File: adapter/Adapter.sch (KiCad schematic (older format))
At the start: 58 parts, among them J1 USB_B_Micro, J2 2040210-1, J3 USB_C_Receptacle, J4 Conn_01x05_Male, J5 Conn_01x03_Male, Q1 IRLML2244TRPBF, SW1 RESET, SW2 BOOT, U1 SN75DP119RGYT, U2 LD1117S33TR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

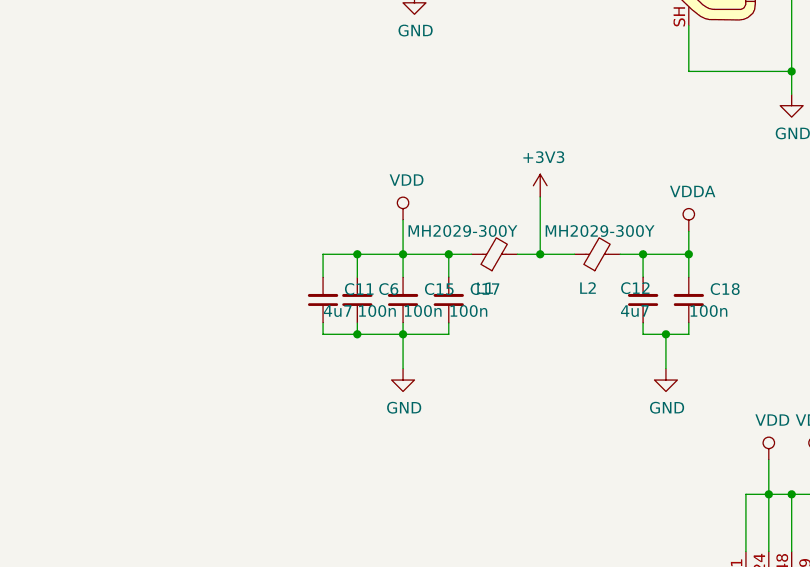
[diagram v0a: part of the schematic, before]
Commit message: shifting back some components from the USB-C jack
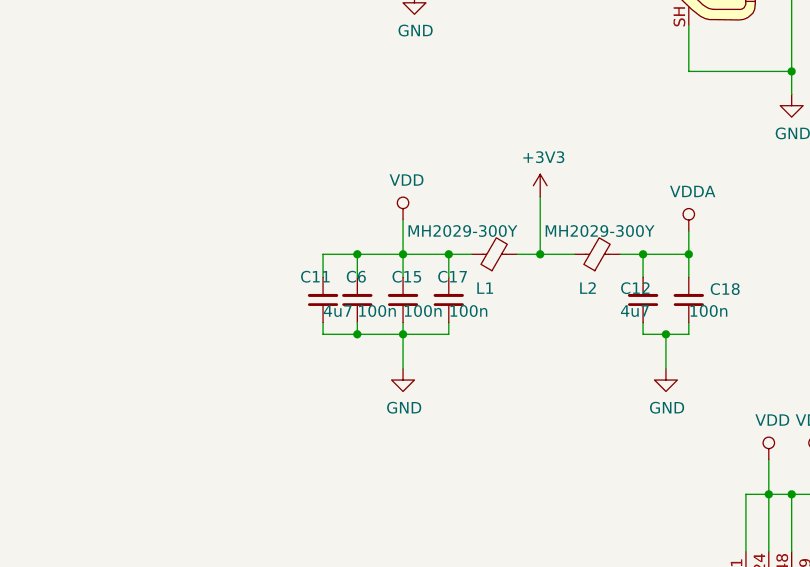
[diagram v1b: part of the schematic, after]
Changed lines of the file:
@@
 U 1 1 5C5D2103
 P 950 3150
-F 0 "C11" H 858 3104 50  0000 R CNN
+F 0 "C11" H 1050 3050 50  0000 R CNN
 F 1 "4u7" H 950 3200 50  0000 R CNN
 F 2 "Capacitor_SMD:C_0603_1608Metric_Pad1.05x0.95mm_HandSolder" H 950 3150 50  0001 C CNN
@@
 U 1 1 5C56A473
 P 1100 3150
-F 0 "C6" H 1008 3104 50  0000 R CNN
+F 0 "C6" H 1150 3050 50  0000 R CNN
 F 1 "100n" H 1100 3200 50  0000 R CNN
 F 2 "Capacitor_SMD:C_0603_1608Metric_Pad1.05x0.95mm_HandSolder" H 1100 3150 50  0001 C CNN
@@
 U 1 1 5C5EEE53
 P 1300 3150
-F 0 "C15" H 1208 3104 50  0000 R CNN
+F 0 "C15" H 1350 3050 50  0000 R CNN
 F 1 "100n" H 1300 3200 50  0000 R CNN
 F 2 "Capacitor_SMD:C_0603_1608Metric_Pad1.05x0.95mm_HandSolder" H 1300 3150 50  0001 C CNN
@@
 U 1 1 5C5EEED5
 P 1500 3150
-F 0 "C17" H 1408 3104 50  0000 R CNN
+F 0 "C17" H 1550 3050 50  0000 R CNN
 F 1 "100n" H 1500 3200 50  0000 R CNN
 F 2 "Capacitor_SMD:C_0603_1608Metric_Pad1.05x0.95mm_HandSolder" H 1500 3150 50  0001 C CNN

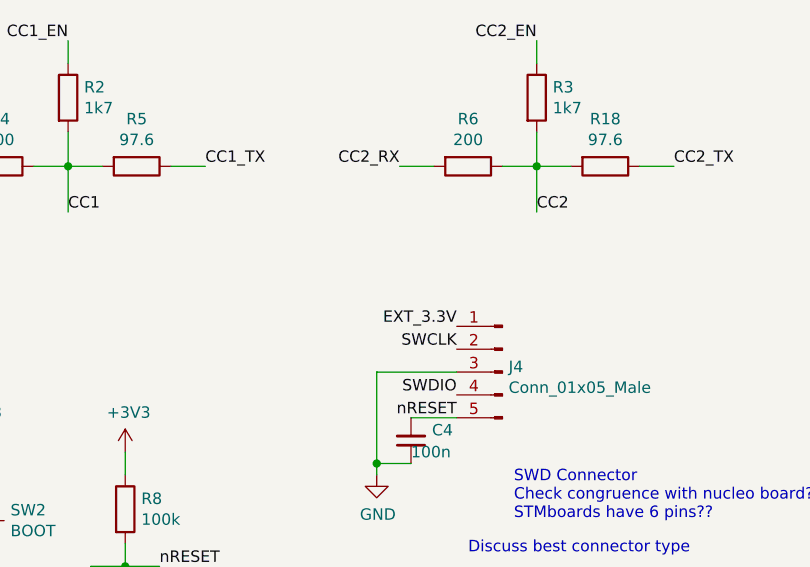
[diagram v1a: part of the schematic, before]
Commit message: Connect EXT3.3V to 3.3V
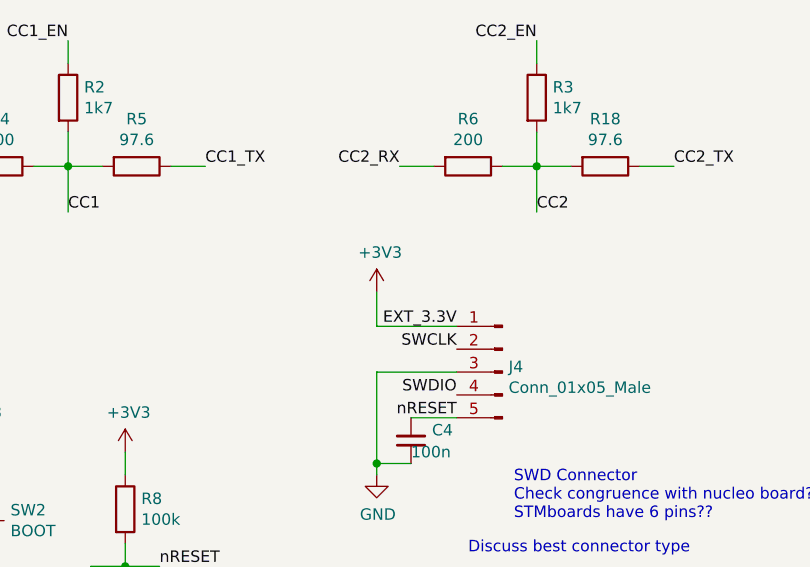
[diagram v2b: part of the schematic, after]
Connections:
- net EXT_3.3V is gone; now on net +3V3: J4.1 (Pin_1)
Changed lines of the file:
@@
 	2100 6350 2300 6350
 NoConn ~ 3350 3250
+$Comp
+L power:+3V3 #PWR?
+U 1 1 5C6DA0CA
+P 6700 4800
+F 0 "#PWR?" H 6700 4650 50  0001 C CNN
+F 1 "+3V3" H 6715 4973 50  0000 C CNN
+F 2 "" H 6700 4800 50  0001 C CNN
+F 3 "" H 6700 4800 50  0001 C CNN
+	1    6700 4800
+	1    0    0    -1
+$EndComp
+Wire Wire Line
+	6700 4800 6700 4950
+Wire Wire Line
+	6700 4950 7050 4950
 $EndSCHEMATC

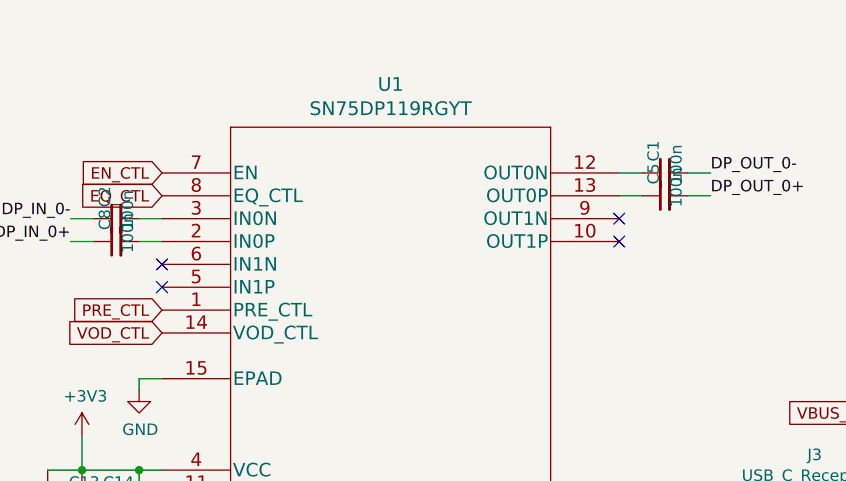
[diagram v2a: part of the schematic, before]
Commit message: retraced impedance critical paths
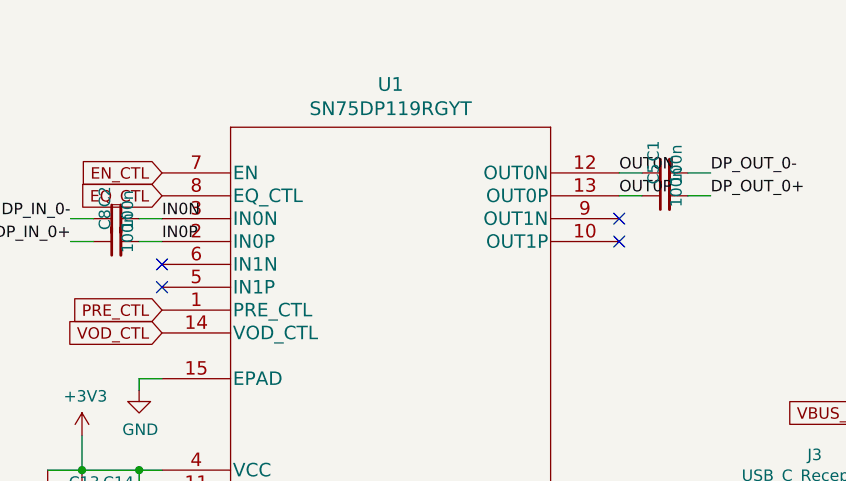
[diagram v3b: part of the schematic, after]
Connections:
- net IN0N: now reaches C2.2, U1.3 (IN0N)
- net IN0P: now reaches C8.2, U1.2 (IN0P)
- net OUT0N: now reaches C1.1, U1.12 (OUT0N)
- net OUT0P: now reaches C5.1, U1.13 (OUT0P)
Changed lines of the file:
@@
 NoConn ~ 3350 3250
 $Comp
-L power:+3V3 #PWR?
+L power:+3V3 #PWR0132
 U 1 1 5C6DA0CA
 P 6700 4800
-F 0 "#PWR?" H 6700 4650 50  0001 C CNN
+F 0 "#PWR0132" H 6700 4650 50  0001 C CNN
 F 1 "+3V3" H 6715 4973 50  0000 C CNN
 F 2 "" H 6700 4800 50  0001 C CNN
@@
 Wire Wire Line
 	6700 4950 7050 4950
+Text Label 6700 1400 0    50   ~ 0
+IN0P
+Text Label 6700 1300 0    50   ~ 0
+IN0N
+Text Label 8700 1100 0    50   ~ 0
+OUT0N
+Text Label 8700 1200 0    50   ~ 0
+OUT0P
 $EndSCHEMATC

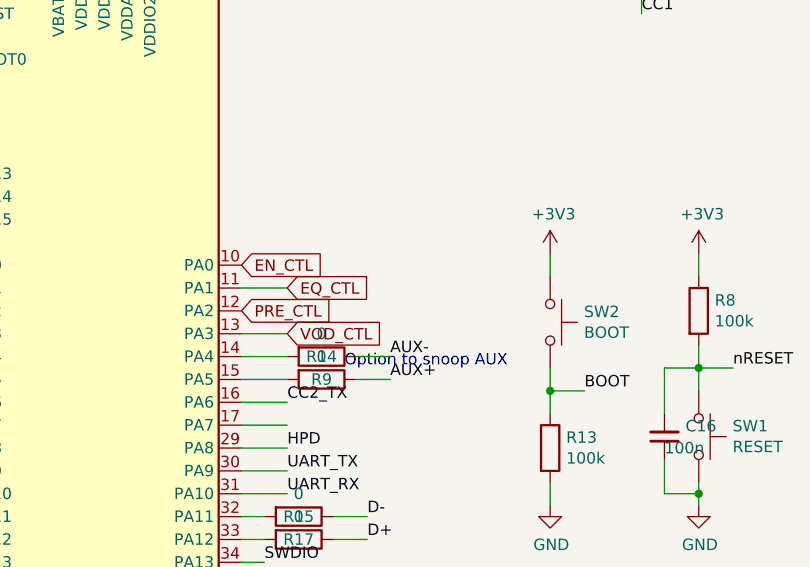
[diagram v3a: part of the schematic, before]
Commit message: fix the PA1 connection (the cheap way, as in prototype)
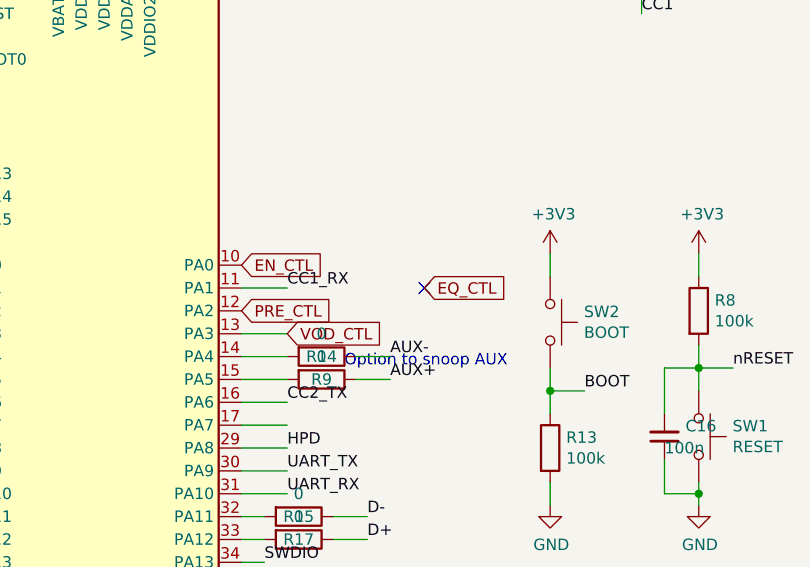
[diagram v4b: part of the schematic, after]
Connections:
- net CC1_RX: now also U3.11 (PA1)
- net EQ_CTL: no longer U3.11 (PA1)
- no-connect marks 17 -> 18
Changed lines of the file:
@@
 EESchema Schematic File Version 4
 LIBS:Adapter-cache
-EELAYER 26 0
+EELAYER 29 0
 EELAYER END
 $Descr A4 11693 8268
@@
 Wire Wire Line
 	1100 6000 1100 6150
-Text GLabel 3800 5650 2    50   Input ~ 0
+Text GLabel 4400 5650 2    50   Input ~ 0
 EQ_CTL
 Text GLabel 3600 5550 2    50   Input ~ 0
@@
 Text Label 8700 1200 0    50   ~ 0
 OUT0P
+NoConn ~ 4400 5650
+Text Label 3800 5650 0    50   ~ 0
+CC1_RX
 $EndSCHEMATC

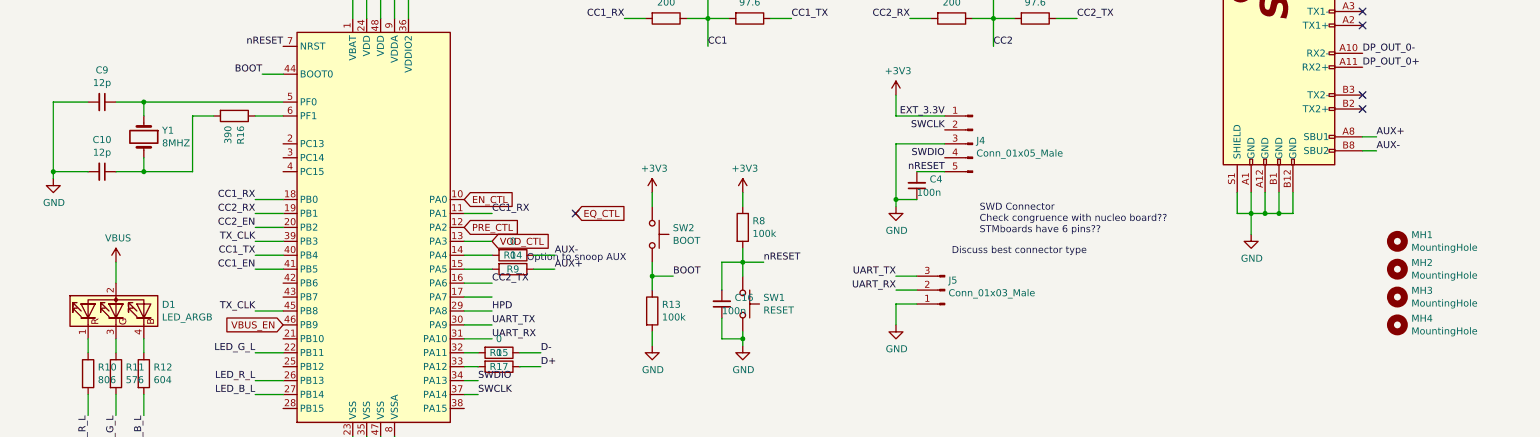
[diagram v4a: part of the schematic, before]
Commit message: enter unpopulated parts note
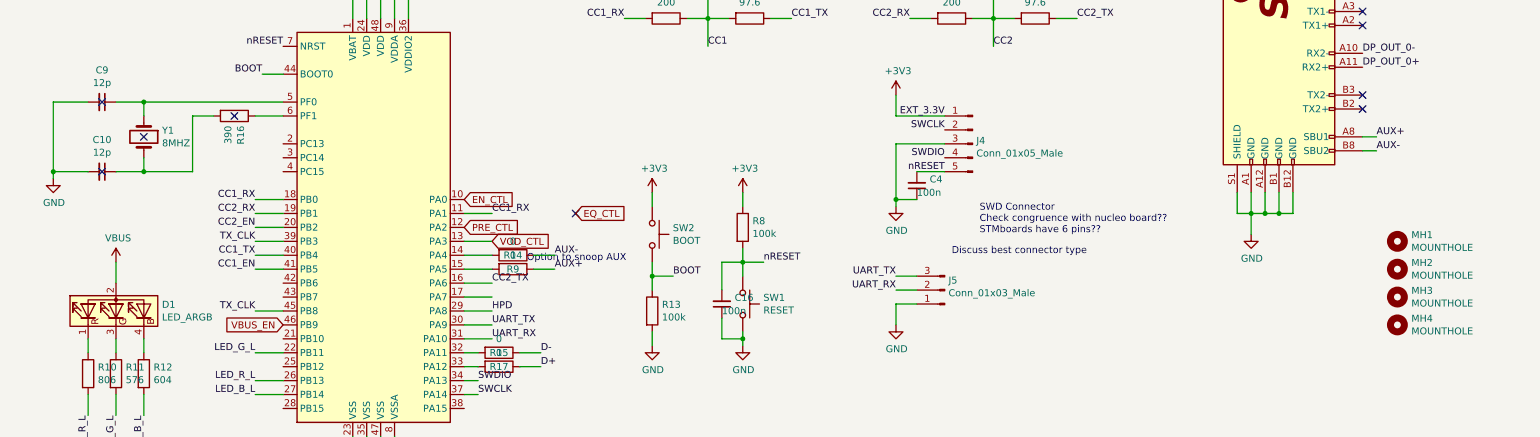
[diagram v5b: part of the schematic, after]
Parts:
- C10, C9, CC1, CC2, J4, J5, R16, Y1: Installed (none) -> NU
- MH1, MH2, MH3, MH4: value MountingHole -> MOUNTHOLE
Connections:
- no-connect marks 18 -> 22
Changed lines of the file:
@@
 F 2 "TestPoint:TestPoint_Pad_D1.0mm" H 10650 3200 50  0001 C CNN
 F 3 "~" H 10650 3200 50  0001 C CNN
+F 4 "NU" H 10650 3200 50  0001 C CNN "Installed"
 	1    10650 3200
 	1    0    0    -1
@@
 F 2 "TestPoint:TestPoint_Pad_D1.0mm" H 10650 3100 50  0001 C CNN
 F 3 "~" H 10650 3100 50  0001 C CNN
+F 4 "NU" H 10650 3100 50  0001 C CNN "Installed"
 	1    10650 3100
 	1    0    0    -1
@@
 F 2 "Connector_PinHeader_2.54mm:PinHeader_1x05_P2.54mm_Horizontal" H 7250 5150 50  0001 C CNN
 F 3 "~" H 7250 5150 50  0001 C CNN
+F 4 "NU" H 7250 5150 50  0001 C CNN "Installed"
 	1    7250 5150
 	-1   0    0    -1
@@
 F 3 "~" H 1300 5100 50  0001 C CNN
 F 4 "7A-8.000MAAE-T" H 1300 5100 50  0001 C CNN "S2PN"
+F 5 "NU" V 1300 5100 50  0001 C CNN "Installed"
 	1    1300 5100
 	0    1    1    0
@@
 F 4 "CL10C120JB8NNNC" H 1000 4850 50  0001 C CNN "MFP"
 F 5 "CL10C120JB8NNNC" V 1000 4850 50  0001 C CNN "S2PN"
+F 6 "NU" V 1000 4850 50  0001 C CNN "Installed"
 	1    1000 4850
 	0    1    1    0
@@
 F 4 "CL10C120JB8NNNC" H 1000 5350 50  0001 C CNN "MFP"
 F 5 "CL10C120JB8NNNC" V 1000 5350 50  0001 C CNN "S2PN"
+F 6 "NU" V 1000 5350 50  0001 C CNN "Installed"
 	1    1000 5350
 	0    1    1    0
@@
 F 4 "RC0603JR-07390RL" H 1950 4950 50  0001 C CNN "MFP"
 F 5 "RC0603JR-07390RL" H 1950 4950 50  0001 C CNN "S2PN"
+F 6 "NU" H 1950 4950 50  0001 C CNN "Installed"
 	1    1950 4950
 	0    1    1    0
@@
 F 2 "Connector_PinHeader_2.54mm:PinHeader_1x03_P2.54mm_Horizontal" H 7050 6200 50  0001 C CNN
 F 3 "~" H 7050 6200 50  0001 C CNN
+F 4 "NU" H 7050 6200 50  0001 C CNN "Installed"
 	1    7050 6200
 	-1   0    0    1
@@
 P 10300 5850
 F 0 "MH1" H 10400 5896 50  0000 L CNN
-F 1 "MountingHole" H 10400 5805 50  0000 L CNN
+F 1 "MOUNTHOLE" H 10400 5805 50  0000 L CNN
 F 2 "MountingHole:MountingHole_2.5mm" H 10300 5850 50  0001 C CNN
 F 3 "~" H 10300 5850 50  0001 C CNN
@@
 P 10300 6050
 F 0 "MH2" H 10400 6096 50  0000 L CNN
-F 1 "MountingHole" H 10400 6005 50  0000 L CNN
+F 1 "MOUNTHOLE" H 10400 6005 50  0000 L CNN
 F 2 "MountingHole:MountingHole_2.5mm" H 10300 6050 50  0001 C CNN
 F 3 "~" H 10300 6050 50  0001 C CNN
@@
 P 10300 6250
 F 0 "MH3" H 10400 6296 50  0000 L CNN
-F 1 "MountingHole" H 10400 6205 50  0000 L CNN
+F 1 "MOUNTHOLE" H 10400 6205 50  0000 L CNN
 F 2 "MountingHole:MountingHole_2.5mm" H 10300 6250 50  0001 C CNN
 F 3 "~" H 10300 6250 50  0001 C CNN
@@
 P 10300 6450
 F 0 "MH4" H 10400 6496 50  0000 L CNN
-F 1 "MountingHole" H 10400 6405 50  0000 L CNN
+F 1 "MOUNTHOLE" H 10400 6405 50  0000 L CNN
 F 2 "MountingHole:MountingHole_2.5mm" H 10300 6450 50  0001 C CNN
 F 3 "~" H 10300 6450 50  0001 C CNN
@@
 Text Label 3800 5650 0    50   ~ 0
 CC1_RX
+NoConn ~ 1950 4950
+NoConn ~ 1300 5100
+NoConn ~ 1000 4850
+NoConn ~ 1000 5350
 $EndSCHEMATC
